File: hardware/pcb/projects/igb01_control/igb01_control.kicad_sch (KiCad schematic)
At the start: 263 parts, among them J1 CODEC_LEFT, J2 CODEC_RIGHT, J3 LEFT_CON, J4 RIGHT_CON, J5 POWER_CON, J6 LED_CON_L, J7 LED_CON_R, J8 SWD_CON, SW59 SW_Push, SW60 SW_Push, SW61 SW_Push, SW62 SW_Push, SW63 SW_Push, SW64 SW_Push, SW65 SW_Push, SW66 SW_Push, SW67 SW_Push, SW68 SW_Push, SW69 SW_Push, SW70 SW_Push, SW71 SW_Push, SW72 SW_Push, SW73 SW_Push, SW74 SW_Push, SW75 SW_Push, SW76 SW_Push, U1 R-78B5.0-2.0, U10 LDK320M18R, U11 TL071H, U2 SSP7603P33PR, U3 STM32G431RBTx, U4 IS31FL3731-SA, U5 TMUX4051, U6 TMUX4051, U7 TMUX4051, U8 MCP33151, U9 SSP7603P33PR, Y1 12MHz

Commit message: update igb01 control board schematic
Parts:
- removed D4: BAT54S, Package_TO_SOT_SMD:SOT-23, symbol Diode:BAT54S
- added C51, C52, C53, C54, C55, C56, C57, C58, C59, C60, C65, C66, C67, C68, C75, C76, C78, C80, C81, C83, C84, C86: 100n, Capacitor_SMD:C_0402_1005Metric, symbol C_Quencer2-led-rescue:C_Small-cqd_touch_pad
- added C61, C62, C63, C64, C87, C88: 18p, Capacitor_SMD:C_0402_1005Metric, symbol C_Quencer2-led-rescue:C_Small-cqd_touch_pad
- added C69, C70, C71, C72: 8p, Capacitor_SMD:C_0402_1005Metric, symbol C_Quencer2-led-rescue:C_Small-cqd_touch_pad
- added C73: 150n, Capacitor_SMD:C_0402_1005Metric, symbol C_Quencer2-led-rescue:C_Small-cqd_touch_pad
- added C74, C77, C79, C82: 220p, Capacitor_SMD:C_0402_1005Metric, symbol C_Quencer2-led-rescue:C_Small-cqd_touch_pad
- added C85: 1u, symbol Device:C_Small
- added D4: 1N4148, symbol Device:D_Small
- added FB4: FerriteBead_Small, symbol Device:FerriteBead_Small
- added J10: ST_JACK_IGB_OUT, symbol thonkicon_stereo:THONKICONN_STEREO
- added J11: USB_C_Receptacle_USB2.0_16P, symbol Connector:USB_C_Receptacle_USB2.0_16P
- added J12: USB_A, symbol Connector:USB_A
- added J13: Micro_SD_Card, symbol Connector:Micro_SD_Card
- added J14: ST_JACK_IGB_IN, symbol thonkicon_stereo:THONKICONN_STEREO
- added J15: ST_JACK_MIDI_OUT, symbol thonkicon_stereo:THONKICONN_STEREO
- added J16: ST_JACK_MIDI_IN, symbol thonkicon_stereo:THONKICONN_STEREO
- added J17: JACK_RST_OUT, symbol thonkiconn:THONKICONN
- added J18: JACK_CV1_IN, symbol thonkiconn:THONKICONN
- added J19: JACK_CV2_IN, symbol thonkiconn:THONKICONN
- added J20: JACK_CV1_OUT, symbol thonkiconn:THONKICONN
- added J21: JACK_CV2_OUT, symbol thonkiconn:THONKICONN
- added J22: JACK_CV3_OUT, symbol thonkiconn:THONKICONN
- added J23: JACK_CV4_OUT, symbol thonkiconn:THONKICONN
- added J24: JACK_SND_L_OUT, symbol thonkiconn:THONKICONN
- added J25: JACK_SND_R_OUT, symbol thonkiconn:THONKICONN
- added J26: JACK_RTN_L_IN, symbol thonkiconn:THONKICONN
- added J27: JACK_RTN_R_IN, symbol thonkiconn:THONKICONN
- added J28: JACK_MAIN_L_OUT, symbol thonkiconn:THONKICONN
- added J29: JACK_MAIN_R_OUT, symbol thonkiconn:THONKICONN
- added J30: JACK_EXT_L_IN, symbol thonkiconn:THONKICONN
- added J31: JACK_EXT_R_IN, symbol thonkiconn:THONKICONN
- added J32: LINE_L_OUT, symbol Connector_Generic:Conn_01x02
- added J33: LINE_R_OUT, symbol Connector_Generic:Conn_01x02
- added J34: ST_JACK_PHONE_OUT, symbol thonkicon_stereo:THONKICONN_STEREO
- added J35, J36: TYPE_SELECT, symbol Connector_Generic:Conn_02x02_Odd_Even
- added J9: JACK_CLK_OUT, symbol thonkiconn:THONKICONN
- added R100, R101, R57, R59, R68, R70, R75, R80, R98, R99: 20k, Resistor_SMD:R_0603_1608Metric, symbol Device:R
- added R102, R103, R94, R95: 47, Resistor_SMD:R_0603_1608Metric, symbol Device:R
- added R22, R23, R24, R25, R26: 47k, Resistor_SMD:R_0603_1608Metric, symbol C_Quencer2-led-rescue:R-cqd_touch_pad
- added R27, R28: 5.1k, Resistor_SMD:R_0603_1608Metric, symbol C_Quencer2-led-rescue:R-cqd_touch_pad
- added R29, R30, R31, R32: 150, symbol Device:R
- added R33: 10k, Resistor_SMD:R_0603_1608Metric, symbol C_Quencer2-led-rescue:R-cqd_touch_pad
- added R34, R35, R38, R39: 220, Resistor_SMD:R_0603_1608Metric, symbol C_Quencer2-led-rescue:R-cqd_touch_pad
- added R36, R37, R50, R51, R52, R53: 1k, Resistor_SMD:R_0603_1608Metric, symbol C_Quencer2-led-rescue:R-cqd_touch_pad
- added R40, R42, R44, R47, R49, R55, R86, R88, R90, R91: 100k, Resistor_SMD:R_0603_1608Metric, symbol Device:R
- added R41, R43, R45, R46, R48, R54, R65, R66, R73, R74, R78, R79, R83, R84: 10k, Resistor_SMD:R_0603_1608Metric, symbol Device:R
- added R56, R58: 200k, Resistor_SMD:R_0603_1608Metric, symbol Device:R
- added R60, R61, R62, R63, R64: 47k, symbol Device:R
- added R67, R72, R77, R82: 5K, Resistor_SMD:R_0603_1608Metric, symbol Device:R
- added R69, R71, R76, R81, R96, R97: 1k, Resistor_SMD:R_0603_1608Metric, symbol Device:R
- added R85: 3.3k, Resistor_SMD:R_0603_1608Metric, symbol C_Quencer2-led-rescue:R-cqd_touch_pad
- added R87, R89, R92, R93: 33k, Resistor_SMD:R_0603_1608Metric, symbol Device:R
- added U12: 74AHCT1G125, symbol 74xGxx:74AHCT1G125
- added U13: TLP2361, Package_SO:SO-5-6_4.55x3.7mm_P1.27mm, symbol Isolator:TLP2310
- added U14, U15, U17, U18: TL074, symbol Amplifier_Operational:TL074
- added U16: DAC8165, Package_SO:TSSOP-16_4.4x5mm_P0.65mm, symbol Analog_DAC:DAC8165
- added U19: MCP6002, symbol Amplifier_Operational:TL072
- added U20: LM4040DBZ-5, Package_TO_SOT_SMD:SOT-23, symbol Reference_Voltage:LM4040DBZ-5
- added U21: OPA2156, symbol Amplifier_Operational:TL072
- U11: value TL071H -> MCP6001
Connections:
- net +12V: now also C65.1, C67.1, C75.1, C80.1, C84.1, U14.4 (V+), U15.4 (V+), U17.4 (V+), U18.4 (V+), U21.8 (V+); no longer C41.1, U11.2 (V-)
- net +3.3V: now also C59.1, C60.1, J13.4 (VDD), R22.2, R23.2, R24.2, R25.2, R26.2, R60.2, R61.2, R62.2, R63.2, R64.2, U13.6 (VDD), U16.12 (IOVDD)
- net +3.3VA: now also C41.1, RV10.4, RV11.4, RV12.4, RV9.4, U11.5 (V+), C83.1, U19.8 (V+)
- net +5V: now also C42.1, C78.1, FB4.2, J36.4 (Pin_4), U12.5 (VCC), U16.4 (AVDD)
- net -12V: now also C66.2, C68.2, C76.2, C81.2, C86.2, R85.2, U14.11 (V-), U15.11 (V-), U17.11 (V-), U18.11 (V-), U21.4 (V-); no longer C42.2, U11.5 (V+)
- net CORE_ADC1_INP1: now also R94.1
- net CORE_ADC2_INP18: now also R95.1
- net CORE_SDMMC3_CK: now also J13.5 (CLK)
- net CORE_SDMMC3_CMD: now also J13.3 (CMD), R24.1
- net CORE_SDMMC3_D0: now also J13.7 (DAT0), R25.1
- net CORE_SDMMC3_D1: now also J13.8 (DAT1), R26.1
- net CORE_SDMMC3_D2: now also J13.1 (DAT2), R22.1
- net CORE_SDMMC3_D3: now also J13.2 (DAT3/CD), R23.1
- net CORE_SPI2_MOSI: now also R62.1, U16.11 (DIN)
- net CORE_SPI2_NSS: now also R61.1, U16.9 (~{SYNC})
- net CORE_SPI2_SCK: now also U16.10 (SCLK)
- net CORE_USART1_RX: now also R31.2
- net CORE_USART1_TX: now also R32.2
- net CORE_USART3_RX: now also U13.5 (VO)
- net CORE_USART3_TX: now also R33.2, U12.2
- net CORE_USART4_RX: now also R29.2
- net CORE_USART4_TX: now also R30.2
- net CORE_USB_DEV_D+: now also J11.A7 (D-), J11.B7 (D-)
- net CORE_USB_DEV_D-: now also J11.A6 (D+), J11.B6 (D+)
- net CORE_USB_HOST_D+: now also J12.3 (D+)
- net CORE_USB_HOST_D-: now also J12.2 (D-)
- net GND: now also C42.2, C59.2, C60.2, J10.1 (GND), J11.A1 (GND), J11.A12 (GND), J11.B1 (GND), J11.B12 (GND), J11.S1 (SHIELD), J12.4 (GND), J12.5 (Shield), J13.6 (VSS), J13.9 (SHIELD), J14.1 (GND), J15.1 (GND), J16.1 (GND), J17.1 (GND), J9.1 (GND), R27.1, R28.1, R33.1, U12.1, U12.3 (GND), U13.4 (GND)
- net GNDA: now also RV10.2, RV11.2, RV12.2, RV9.2, U11.2 (V-), C51.2, C52.2, C53.2, C54.2, C55.2, C56.2, C57.2, C58.2, C65.2, C66.1, C67.2, C68.1, C73.1, C75.2, C76.1, C78.2, C80.2, C81.1, C83.2, C84.2, C85.2, C86.1, J18.1 (GND), J18.2 (SW), J19.1 (GND), J19.2 (SW), J20.1 (GND), J21.1 (GND), J22.1 (GND), J23.1 (GND), J26.1 (GND), J26.2 (SW), J27.1 (GND), J27.2 (SW), J30.1 (GND), J30.2 (SW), J31.1 (GND), J31.2 (SW), J32.2 (Pin_2), J33.2 (Pin_2), J34.1 (GND), U14.10 (+), U14.12 (+), U14.3 (+), U14.5 (+), U15.10 (+), U15.12 (+), U15.3 (+), U15.5 (+), U16.15 (~{ENABLE}), U16.5 (VREFL), U16.6 (GND), U17.12 (+), U17.5 (+), U18.12 (+), U18.5 (+), U19.3 (+), U19.4 (V-), U19.5 (+), U20.1 (K), U21.3 (+); no longer C42.1
- net IN1L: now also C61.2, R41.1, U14.1
- net IN1R: now also C62.2, R43.1, U14.7
- net IN2L: now also C63.2, R45.1, U14.14
- net IN2R: now also C64.2, R46.1, U14.8
- net OUT1L: now also R48.2
- net OUT1R: now also R54.2
- net OUT2L: now also R57.2, R98.2
- net OUT2R: now also R101.2, R59.2
- net PARAM_KNOB1_A: now also RV9.1, C51.1
- net PARAM_KNOB1_B: now also RV9.3, C52.1
- net PARAM_KNOB2_A: now also RV10.1, C53.1
- net PARAM_KNOB2_B: now also RV10.3, C54.1
- net PARAM_KNOB3_A: now also RV11.1, C55.1
- net PARAM_KNOB3_B: now also RV11.3, C56.1
- net PARAM_KNOB4_A: now also RV12.1, C57.1
- net PARAM_KNOB4_B: now also RV12.3, C58.1
- new net: J32.1 (Pin_1), R96.1
- new net: C87.2, R102.2, R96.2, R99.1, U21.1
- new net: C88.1, R100.2, R101.1, U21.6 (-)
- new net: C88.2, R100.1, R103.2, R97.2, U21.7
- new net: J34.3 (TIP), R102.1
- new net: C61.1, R40.1, R41.2, U14.2 (-)
- new net: C82.1, R80.2, R82.1, U18.13 (-)
- new net: R82.2, R83.1, U18.8
- new net: J15.2 (RING), R35.1
- new net: J15.3 (TIP), R34.1
- new net: C70.1, R54.1, R55.2, U15.6 (-)
- new net: C71.1, R56.2, R57.1, U15.9 (-)
- new net: C77.1, R70.2, R72.1, U17.13 (-)
- new net: C77.2, R71.2, U17.14
- new net: J34.2 (RING), R103.1
- new net: R86.1, R87.2, R88.1, R92.2, U19.2 (-)
- new net: C69.1, R48.1, R49.2, U15.2 (-)
- new net: C62.1, R42.1, R43.2, U14.6 (-)
- new net: J16.2 (RING), R39.1
- new net: R87.1, R92.1, R94.2, U19.1
- new net: R65.1, R66.2, U17.2 (-)
- new net: J14.2 (RING), R32.1
- new net: J14.3 (TIP), R31.1
- new net: J29.3 (TIP), R53.1
- new net: C79.2, R76.2, U18.7
- new net: J10.2 (RING), R29.1
- new net: J36.2 (Pin_2), U12.4
- new net: D4.1 (K), J35.1 (Pin_1), U13.1 (A)
- new net: D4.2 (A), J35.3 (Pin_3), U13.3 (K)
- new net: R77.2, R78.1, U18.1
- new net: R78.2, R79.1, U18.2 (-)
- new net: C63.1, R44.1, R45.2, U14.13 (-)
- new net: C74.2, R69.2, U17.7
- new net: C64.1, R46.2, R47.1, U14.9 (-)
- new net: J25.3 (TIP), R51.1
- new net: C79.1, R75.2, R77.1, U18.6 (-)
- new net: C87.1, R98.1, R99.2, U21.2 (-)
- new net: J9.3 (TIP), R36.1
- new net: R72.2, R73.1, U17.8
- new net: R73.2, R74.1, U17.9 (-)
- new net: R83.2, R84.1, U18.9 (-)
- new net: R89.2, R90.1, R91.1, R93.2, U19.6 (-)
- new net: J16.3 (TIP), R38.1
- new net: J24.3 (TIP), R50.1
- new net: C72.1, R58.2, R59.1, U15.13 (-)
- new net: J33.1 (Pin_1), R97.1
- new net: C74.1, R67.1, R68.2, U17.6 (-)
- new net: R89.1, R93.1, R95.2, U19.7
- new net: R66.1, R67.2, U17.1
- new net: R64.1, U16.13 (~{RST})
- new net: R60.1, U16.16 (LDAC)
- new net: J11.A5 (CC1), R27.2
- new net: J10.3 (TIP), R30.1
- new net: J11.B5 (CC2), R28.2
- new net: FB4.1, J12.1 (VBUS)
- new net: J17.3 (TIP), R37.1
- new net: J11.A4 (VBUS), J11.A9 (VBUS), J11.B4 (VBUS), J11.B9 (VBUS)
- new net: C82.2, R81.2, U18.14
- new net: R63.1, U16.14 (RSTSEL)
- new net: J28.3 (TIP), R52.1
- new net CV1_IN: J18.3 (TIP), R86.2
- new net CV1_OUT: J20.3 (TIP), R68.1, R69.1
- new net CV2_IN: J19.3 (TIP), R91.2
- new net CV2_OUT: J21.3 (TIP), R70.1, R71.1
- new net CV3_OUT: J22.3 (TIP), R75.1, R76.1
- new net CV4_OUT: J23.3 (TIP), R80.1, R81.1
- new net DAC_OUT_A: U16.1 (VOUTA), U17.3 (+)
- new net DAC_OUT_B: U16.2 (VOUTB), U17.10 (+)
- new net DAC_OUT_C: U16.7 (VOUTC), U18.3 (+)
- new net DAC_OUT_D: U16.8 (VOUTD), U18.10 (+)
- new net EXT_L_IN: J30.3 (TIP), R44.2
- new net EXT_R_IN: J31.3 (TIP), R47.2
- new net MAIN_L_OUT: C71.2, R52.2, R56.1, U15.8
- new net MAIN_R_OUT: C72.2, R53.2, R58.1, U15.14
- new net MIDI_IN: J35.4 (Pin_4), R38.2
- new net MIDI_IN_VCC: J35.2 (Pin_2), R39.2
- new net MIDI_OUT_RING: J36.3 (Pin_3), R35.2
- new net MIDI_OUT_TIP: J36.1 (Pin_1), R34.2
- new net RTN_L_IN: J26.3 (TIP), R40.2
- new net RTN_R_IN: J27.3 (TIP), R42.2
- new net SND_L_OUT: C69.2, R49.1, R50.2, U15.1
- new net SND_R_OUT: C70.2, R51.2, R55.1, U15.7
- new net VREF_-5V: C85.1, R85.1, R88.2, R90.2, U20.2 (A)
- new net VREF_2.5V: C73.2, R65.2, R74.2, R79.2, R84.2, U16.3 (VREFH/VREFOUT)
- no-connect marks 7 -> 20
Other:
- note added: "916-252A1013Y10200"
- note added: "AUDIO IN Buffer"
- note added: "AUDIO OUT Buffer"
- note added: "CV IN Buffer"
- note added: "DAC Out Buffer"
- note added: "EXT DAC"
- note added: "GT-USB-7038E"
- note added: "Line & Phone Out"
- note added: "MIDI Buffer"
- note added: "PARAM Knobs"
- note added: "PJS008U-3000-0"
- note added: "POWER"
- note added: "SDMMC Card"
- note added: "USB Device"
- note added: "USB Host"
- note removed: "PARAM Buttons"
- note removed: "TODO: Jacks"
- moved on the sheet: C10, C11, C12, C13, C14, C15, C16, C17, C18, C19, C20, C21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

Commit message: update igb01 control schematic
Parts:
- removed C14, C15: 100n, Capacitor_SMD:C_0402_1005Metric, symbol C_Quencer2-led-rescue:C_Small-cqd_touch_pad
- removed D21, D22: 1N4148, symbol Device:D_Small
- removed D3: PEAK_LED, symbol Device:LED
- removed J32: LINE_L_OUT, symbol Connector_Generic:Conn_01x02
- removed J33: LINE_R_OUT, symbol Connector_Generic:Conn_01x02
- removed J6: LED_CON_L, symbol Connector_Generic:Conn_01x10
- removed J7: LED_CON_R, symbol Connector_Generic:Conn_01x10
- removed R6: 100k, Resistor_SMD:R_0603_1608Metric, symbol C_Quencer2-led-rescue:R-cqd_touch_pad
- removed R7: 10k, Resistor_SMD:R_0603_1608Metric, symbol C_Quencer2-led-rescue:R-cqd_touch_pad
- removed R8: 47k, Resistor_SMD:R_0603_1608Metric, symbol C_Quencer2-led-rescue:R-cqd_touch_pad
- removed unit 2 of SW1
- removed unit 2 of SW13
- removed unit 2 of SW14
- removed unit 2 of SW15
- removed unit 2 of SW16
- removed unit 2 of SW17
- removed unit 2 of SW18
- removed unit 2 of SW19
- removed unit 2 of SW2
- removed unit 2 of SW20
- removed SW21, SW22: ~, symbol push_sw_w_led:PUSH_SW_LED
- removed unit 2 of SW3
- removed unit 2 of SW39
- removed unit 2 of SW4
- removed unit 2 of SW40
- removed unit 2 of SW41
- removed unit 2 of SW42
- removed unit 2 of SW43
- removed unit 2 of SW44
- removed unit 2 of SW45
- removed unit 2 of SW46
- removed unit 2 of SW5
- removed unit 2 of SW6
- removed unit 2 of SW7
- removed unit 2 of SW8
- removed U4: IS31FL3731-SA, Package_SO:SSOP-28_5.3x10.2mm_P0.65mm, symbol Driver_LED:IS31FL3731-SA
- added Q1, Q2, Q3, Q4, Q5, Q6, Q7, Q8: MMBT3904, Package_TO_SOT_SMD:SOT-23, symbol Transistor_BJT:MMBT3904
- added R104: 10k, Resistor_SMD:R_0603_1608Metric, symbol Device:R
- added R105, R110, R113, R6, R8: 1k, Resistor_SMD:R_0603_1608Metric, symbol Device:R
- added R106, R107, R108, R109, R111, R112, R114, R7: 2.2k, Resistor_SMD:R_0603_1608Metric, symbol Device:R
- added RV13: B10k, symbol Device:R_Potentiometer
- added U4: 74HC595, symbol 74xx:74HC595
- C87, C88: value 18p -> 47p
- R100, R99: value 20k -> 10k
- R101, R98: value 20k -> 1k
- R102, R103: value 47 -> 39
- R96: value 1k -> 10k
- SW1, SW2, SW3, SW4, SW5, SW6, SW7, SW8: symbol push_sw_w_led:PUSH_SW_BI_LED -> Switch:SW_Push
- SW13, SW14, SW15, SW16, SW17, SW18, SW19, SW20, SW39, SW40, SW41, SW42, SW43, SW44, SW45, SW46: symbol push_sw_w_led:PUSH_SW_LED -> Switch:SW_Push
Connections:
- net TOUCH_I2C2_SDA is gone; now on net PARAM_BTN4: U3.42 (PA8)
- net +3.3V: now also C13.2, Q1.3 (C), Q2.3 (C), Q3.3 (C), Q4.3 (C), Q5.3 (C), Q6.3 (C), Q7.3 (C), Q8.3 (C), U4.10 (~{SRCLR}), U4.16 (VCC)
- net +3.3VA: now also RV13.3
- net GND: now also C13.1, R106.2, R107.2, R108.2, R109.2, R111.2, R112.2, R114.2, R7.2, U4.13 (~{OE}), U4.8 (GND); no longer C13.2
- net GNDA: now also U21.5 (+), RV13.1
- net OUT2L: now also R96.2; no longer R98.2
- net OUT2R: now also R104.2; no longer R101.2
- net PARAM_BTN4: no longer U3.44 (PA10)
- net at R96.1: now also C87.1, R99.2, U21.2 (-)
- net at C87.2, R102.2, R99.1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: no longer R96.2
- net at C88.1, R100.2, U21.6 (-): now also R104.1; no longer R101.1
- net at C88.2, R100.1, R103.2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: no longer R97.2
- net at SW9.3: no longer SW10.4
- net at RV3.4: now also Q3.2 (E); no longer RV4.5
- net at SW12.4: no longer SW11.3
- net at R97.1: now also Q5.1 (B)
- net at RV2.5: now also R106.1; no longer RV1.4
- net at RV5.4: now also Q5.2 (E); no longer RV6.5
- net at RV7.4: now also Q7.2 (E); no longer RV8.5
- net SR_SER: now reaches U3.45 (PA11)
- net SR_SER: now also U4.14 (SER)
- net SR_RCLK: now reaches U3.46 (PA12)
- net SR_RCLK: now also U4.12 (RCLK)
- net SR_SRCLK: now reaches U3.51 (PA15)
- net SR_SRCLK: now also U4.11 (SRCLK)
- net RIBBON_ADC_IN renamed VOLUME_ADC_IN
- net VOLUME_ADC_IN: now also RV13.2
- net TOUCH_I2C2_SCL renamed USART1_TX
- new net: Q3.1 (B), R8.1
- new net: Q4.1 (B), R105.1
- new net: R105.2, U4.3 (QD)
- new net: Q7.1 (B), R98.1
- new net: R112.1, RV7.5
- new net: R8.2, U4.2 (QC)
- new net: Q2.1 (B), R101.1
- new net: R101.2, U4.1 (QB)
- new net: R7.1, RV1.5
- new net: Q2.2 (E), RV2.4
- new net: Q4.2 (E), RV4.4
- new net: R108.1, RV4.5
- new net: Q8.1 (B), R113.1
- new net: Q8.2 (E), RV8.4
- new net: Q6.1 (B), R110.1
- new net: R110.2, U4.5 (QF)
- new net: R114.1, RV8.5
- new net: Q6.2 (E), RV6.4
- new net: R111.1, RV6.5
- new net: R107.1, RV3.5
- new net: Q1.1 (B), R6.1
- new net: R6.2, U4.15 (QA)
- new net: R97.2, U4.4 (QE)
- new net: R109.1, RV5.5
- new net: R98.2, U4.6 (QG)
- new net: Q1.2 (E), RV1.4
- new net: R113.2, U4.7 (QH)
- new net USART1_RX: U3.44 (PA10)
- now unconnected: SW10.3, SW11.4, SW12.3, SW23.3, SW23.4, SW24.3, SW24.4, SW25.3, SW25.4, SW26.3, SW26.4, SW27.3, SW27.4, SW28.3, SW28.4, SW29.3, SW29.4, SW30.3, SW30.4, SW31.3, SW31.4, SW32.3, SW32.4, SW33.3, SW33.4, SW34.3, SW34.4, SW35.3, SW35.4, SW36.3, SW36.4, SW37.3, SW37.4, SW38.3, SW38.4, SW47.3, SW47.4, SW48.3, SW48.4, SW49.3, SW49.4, SW50.3, SW50.4, SW51.3, SW51.4, SW52.3, SW52.4, SW53.3, SW53.4, SW54.3, SW54.4, SW55.3, SW55.4, SW56.3, SW56.4, SW57.3, SW57.4, SW58.3, SW58.4, SW9.4
- no-connect marks 20 -> 83
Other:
- note added: "Slider LED"
- note added: "TODO: USBコネクタは別基板に"
- note added: "TODO: use Type A to Type C converter? (MAX20463AGTCA/V+)"
- note added: "Volume"
- note added: "for TOUCH MCU"
- note removed: "C1-10 C3-9"
- note removed: "C1-11 C4-9"
- note removed: "C1-12 C5-9"
- note removed: "C1-13"
- note removed: "C1-14"
- note removed: "C1-15"
- note removed: "C1-16"
- note removed: "C1-8"
- note removed: "C1-9 C2-9"
- note removed: "C2-10 C3-10"
- note removed: "C2-11 C4-10"
- note removed: "C2-12 C5-10"
- note removed: "C2-13"
- note removed: "C2-14"
- note removed: "C2-15"
- note removed: "C2-16"
- note removed: "C2-8"
- note removed: "C3-11 C4-11"
- note removed: "C3-12"
- note removed: "C3-13"
- note removed: "C3-14"
- note removed: "C3-15"
- note removed: "C3-16"
- note removed: "C3-8"
- note removed: "C4-12"
- note removed: "C4-13"
- note removed: "C4-14"
- note removed: "C4-15"
- note removed: "C4-8"
- note removed: "C5-11"
- note removed: "C5-12"
- note removed: "C5-13"
- note removed: "C5-14"
- note removed: "C5-15"
- note removed: "C5-8"
- note removed: "C6-10"
- note removed: "C6-11"
- note removed: "C6-12"
- note removed: "C6-13"
- note removed: "C6-14"
- note removed: "C6-15"
- note removed: "C6-8"
- note removed: "C6-9"
- note removed: "C7-10"
- note removed: "C7-11"
- note removed: "C7-12"
- note removed: "C7-13"
- note removed: "C7-14"
- note removed: "C7-15"
- note removed: "C7-9"
- note removed: "C8-10"
- note removed: "C8-11"
- note removed: "C8-12"
- note removed: "C8-13"
- note removed: "C8-14"
- note removed: "C8-15"
- note removed: "C8-9"
- note removed: "C9-1"
- note removed: "C9-10"
- note removed: "C9-11"
- note removed: "C9-2"
- note removed: "C9-3"
- note removed: "C9-4"
- note removed: "C9-5"
- note removed: "C9-6"
- note removed: "C9-7"
- note removed: "C9-9"
- note removed: "LED Driver"
- note removed: "Macro Knob Button LEDs"
- note removed: "Mixer Fader LEDs"
- note removed: "PEAK LED"
- note removed: "RELATIVE /LATCh LEDs"
- note removed: "RELATIVE/LATCH Buttons"
- note removed: "Ribbon Mode LEDs"
- note removed: "Touch Pad Board Connector"
- note removed: "small illuminated:btn: https://www.thonk.co.uk/shop/low-profile-led-buttons/ large illuminated btn: KS01-BL-5(HIGHLY) or D6RLWHF1LFS(C&K) square illuminat4ed btn: KS01-AL-5"
- moved on the sheet: C84, C86, C87, C88, FB4, J11, J12, J34, R100, R102, R103, R27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

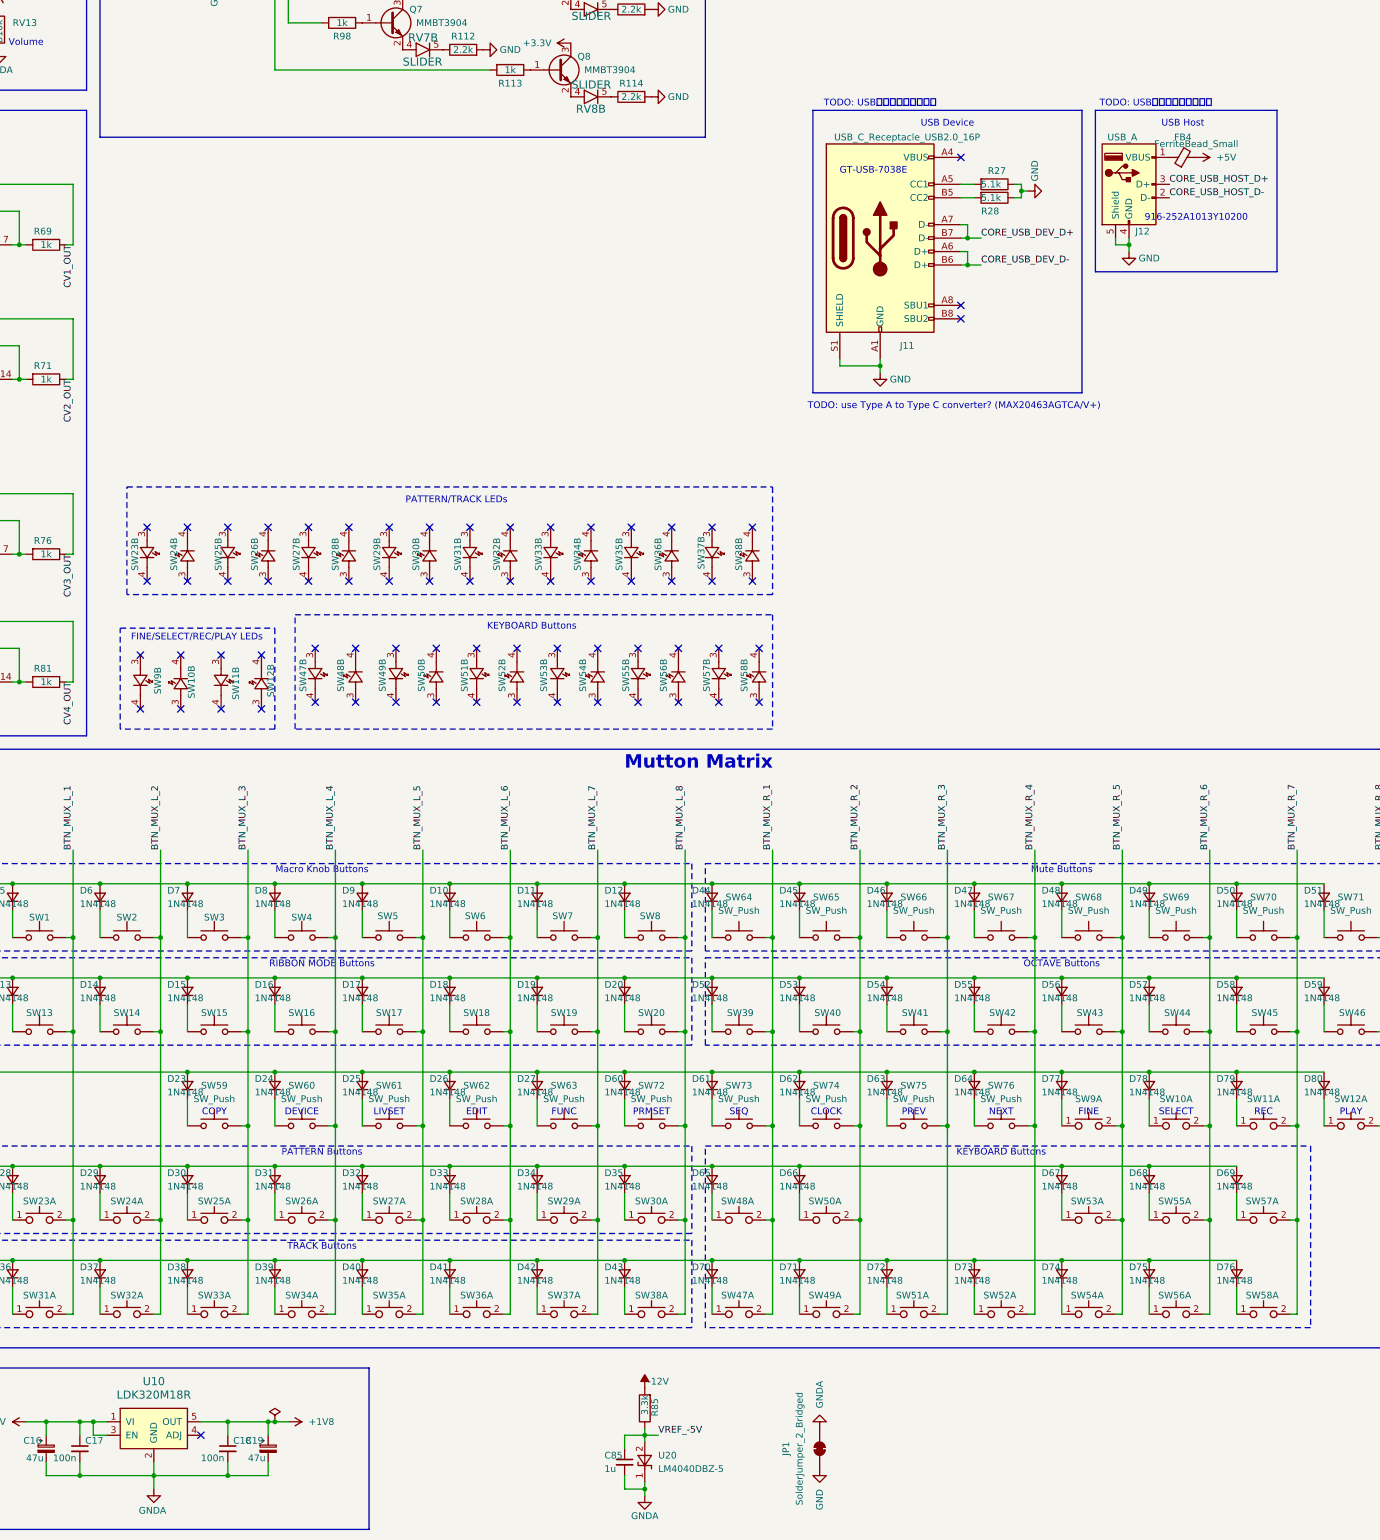
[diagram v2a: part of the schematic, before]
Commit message: update led&control schematics
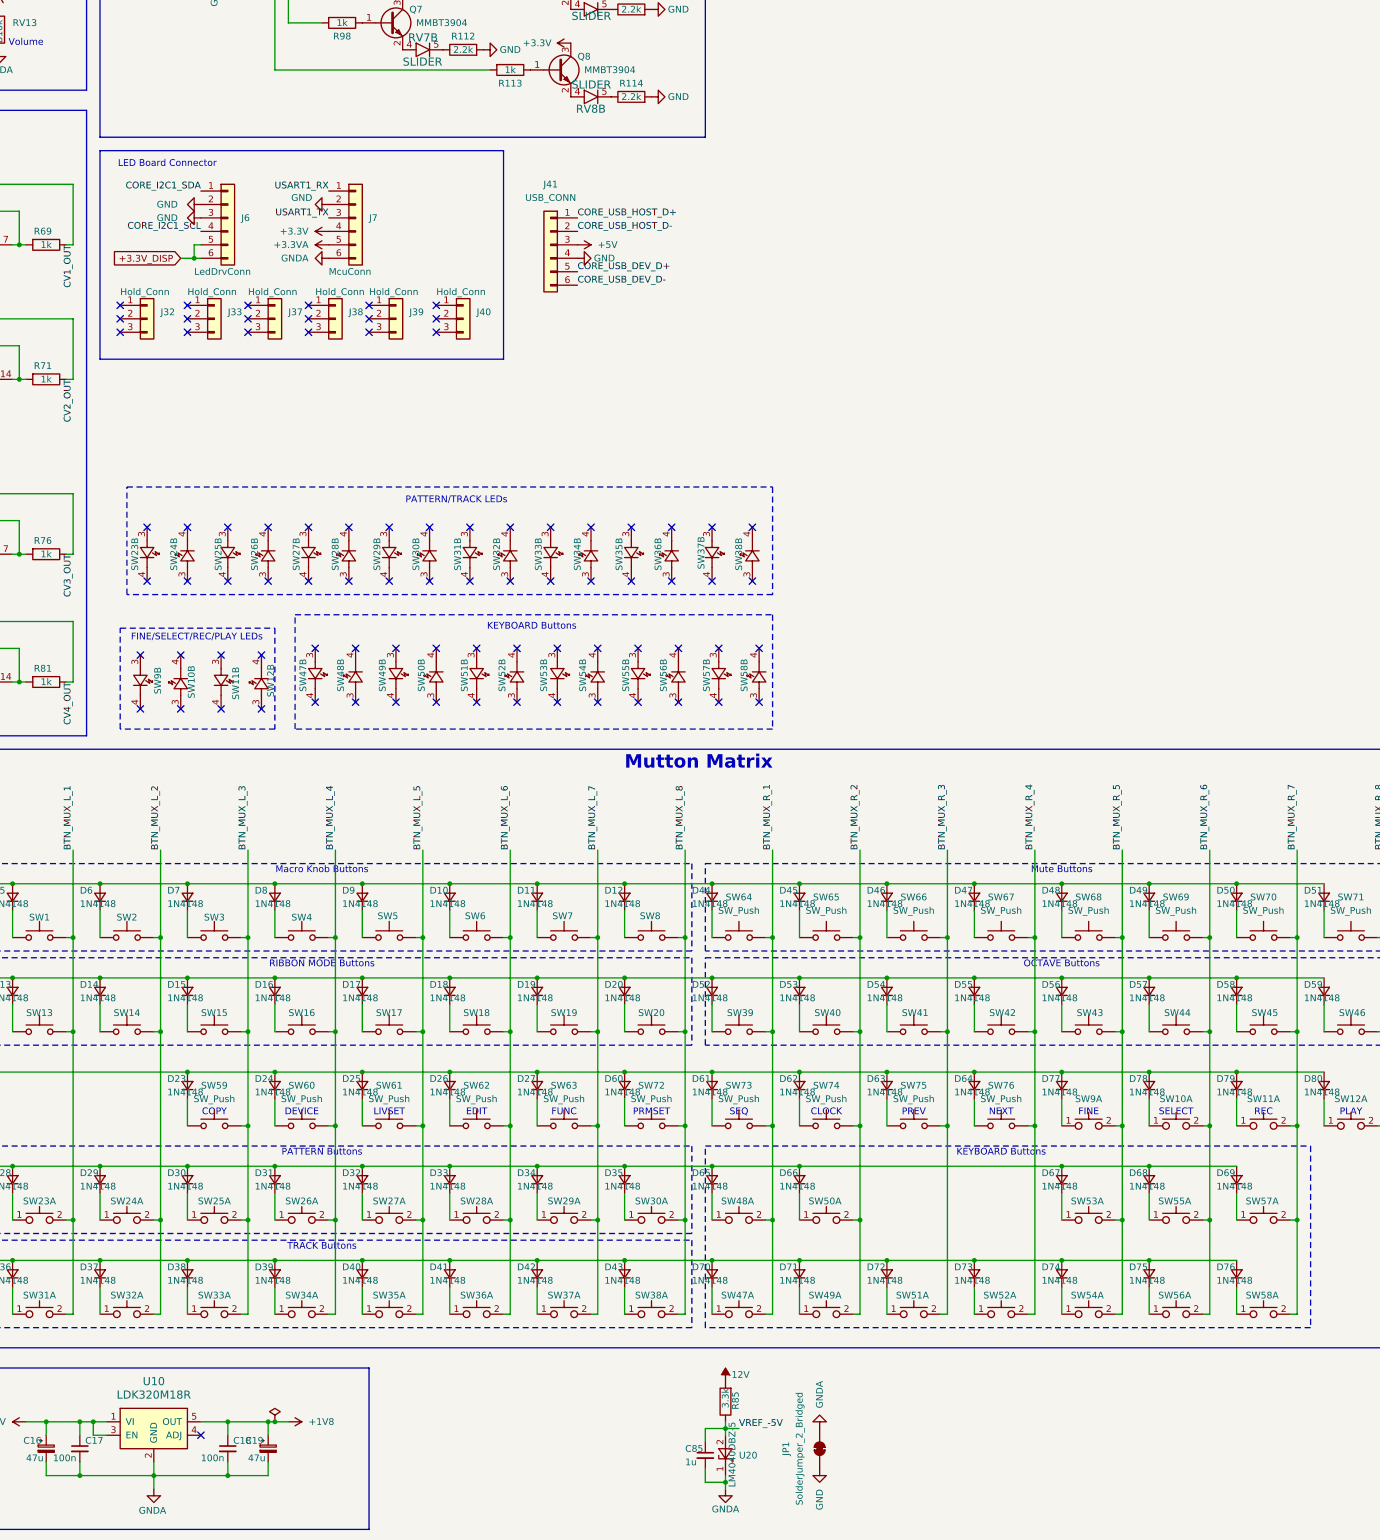
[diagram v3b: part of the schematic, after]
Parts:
- removed FB4: FerriteBead_Small, symbol Device:FerriteBead_Small
- removed J11: USB_C_Receptacle_USB2.0_16P, symbol Connector:USB_C_Receptacle_USB2.0_16P
- removed J12: USB_A, symbol Connector:USB_A
- removed R27, R28: 5.1k, Resistor_SMD:R_0603_1608Metric, symbol C_Quencer2-led-rescue:R-cqd_touch_pad
- added J32, J33, J37, J38, J39, J40: Hold_Conn, Connector_PinSocket_2.00mm:PinSocket_1x03_P2.00mm_Vertical, symbol Connector_Generic:Conn_01x03
- added J41: USB_CONN, Connector_Molex:Molex_KK-254_AE-6410-06A_1x06_P2.54mm_Vertical, symbol Connector_Generic:Conn_01x06
- added J6: LedDrvConn, Connector_PinHeader_2.00mm:PinHeader_1x06_P2.00mm_Vertical, symbol Connector_Generic:Conn_01x06
- added J7: McuConn, Connector_PinHeader_2.00mm:PinHeader_1x06_P2.00mm_Vertical, symbol Connector_Generic:Conn_01x06
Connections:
- net +3.3V: now also J7.4 (Pin_4)
- net +3.3VA: now also J7.5 (Pin_5)
- net +3.3V_DISP: now also J6.5 (Pin_5), J6.6 (Pin_6)
- net +5V: now also J41.3 (Pin_3)
- net CORE_I2C1_SCL: now also J6.4 (Pin_4)
- net CORE_I2C1_SDA: now also J6.1 (Pin_1)
- net CORE_USB_DEV_D+: now also J41.5 (Pin_5)
- net CORE_USB_DEV_D-: now also J41.6 (Pin_6)
- net CORE_USB_HOST_D+: now also J41.1 (Pin_1)
- net CORE_USB_HOST_D-: now also J41.2 (Pin_2)
- net GND: now also J41.4 (Pin_4), J6.2 (Pin_2), J6.3 (Pin_3), J7.2 (Pin_2)
- net GNDA: now also J7.6 (Pin_6)
- net USART1_RX: now also J7.1 (Pin_1)
- net USART1_TX: now also J7.3 (Pin_3)
- no-connect marks 83 -> 98
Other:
- note added: "LED Board Connector"
- note removed: "916-252A1013Y10200"
- note removed: "GT-USB-7038E"
- note removed: "TODO: USBコネクタは別基板に"
- note removed: "TODO: use Type A to Type C converter? (MAX20463AGTCA/V+)"
- note removed: "USB Device"
- note removed: "USB Host"
- moved on the sheet: C85, R85, U20
